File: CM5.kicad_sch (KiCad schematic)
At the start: 1 part

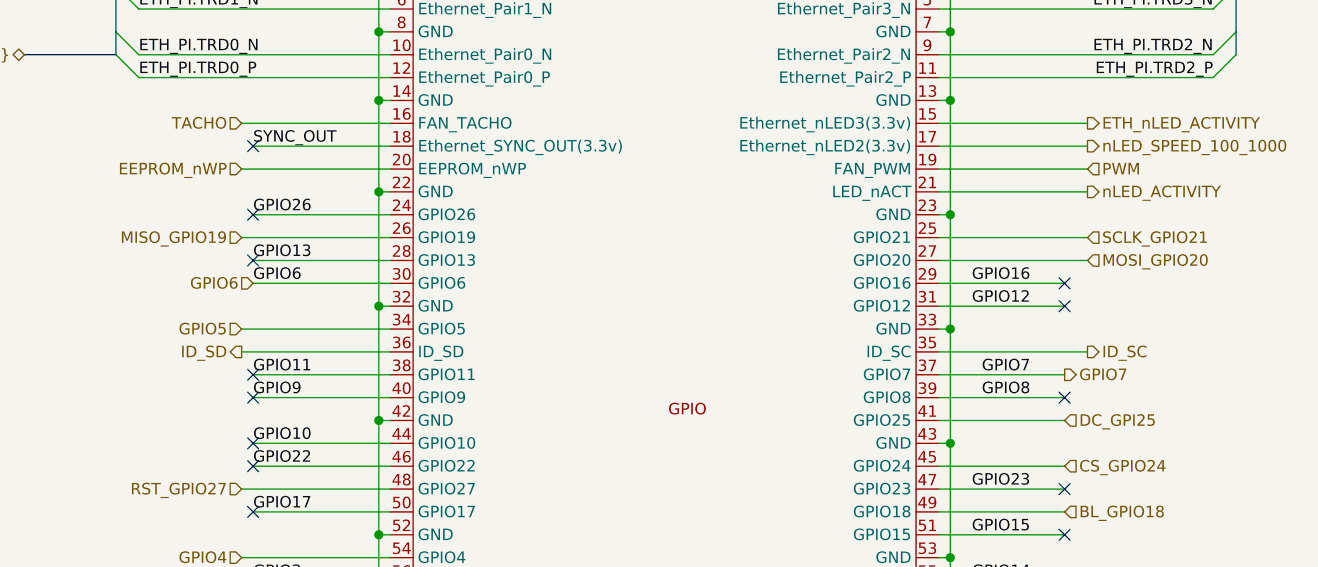
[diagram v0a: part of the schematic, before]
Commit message: Added LiDAR and LCD connections
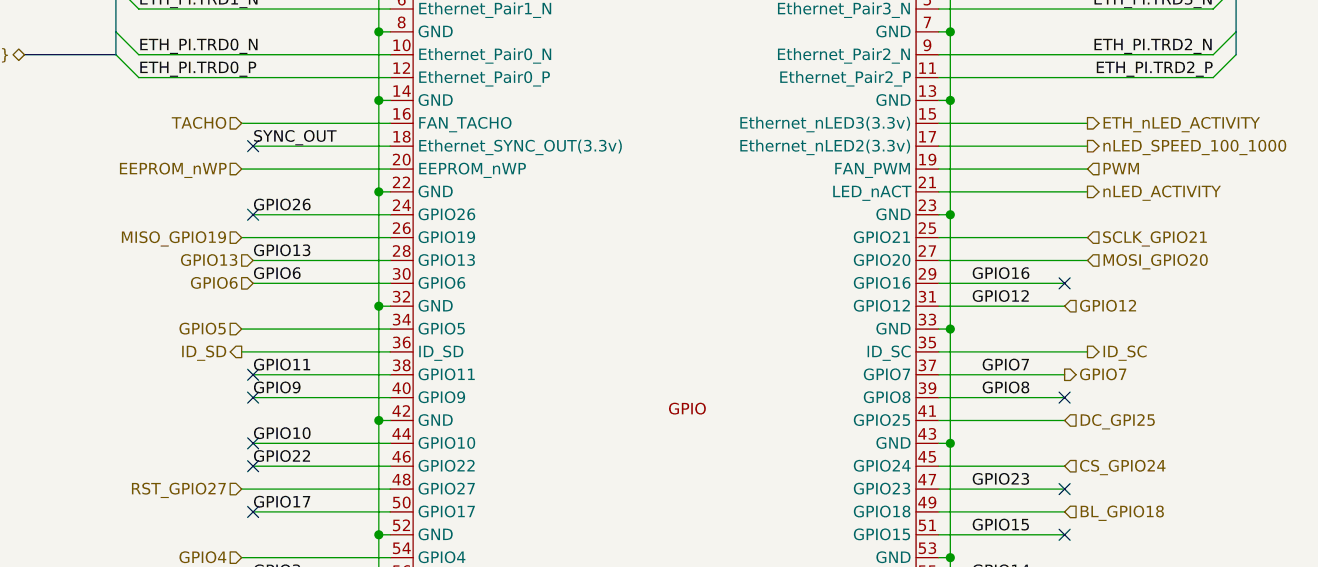
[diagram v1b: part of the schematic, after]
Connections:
- no-connect marks 62 -> 60
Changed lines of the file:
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@@
 	)
 	(no_connect
-		(at 165.1 105.41)
-	)
-	(no_connect
 		(at 351.79 171.45)
 	)
@@
 	)
 	(no_connect
-		(at 74.93 100.33)
-	)
-	(no_connect
 		(at 90.17 151.13)
 	)
@@
 		)
 	)
+	(hierarchical_label "GPIO12"
+		(shape input)
+		(at 165.1 105.41 0)
+		(effects
+			(font
+				(size 1.27 1.27)
+			)
+			(justify left)
+		)
+	)
 	(hierarchical_label "1V8_CM4"
 		(shape output)
@@
 		)
 	)
+	(hierarchical_label "GPIO13"
+		(shape input)
+		(at 74.93 100.33 180)
+		(effects
+			(font
+				(size 1.27 1.27)
+			)
+			(justify right)
+		)
+	)
